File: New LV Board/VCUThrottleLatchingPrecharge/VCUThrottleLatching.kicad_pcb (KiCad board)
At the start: 2 copper layers, 46 x 50.5 mm, 32 parts, among them J1 B12B-PH-K-S:JST_B12B-PH-K-S, P1 PH1-20-UA, P2 PH1-20-UA, Q1 SS8550, U1 IRLML2060TRPBF, U2 IRLML2060TRPBF, U3 IRLML2060TRPBF, U5 IRLML2060TRPBF, U6 IRLML2060TRPBF, U8 PMV160UP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

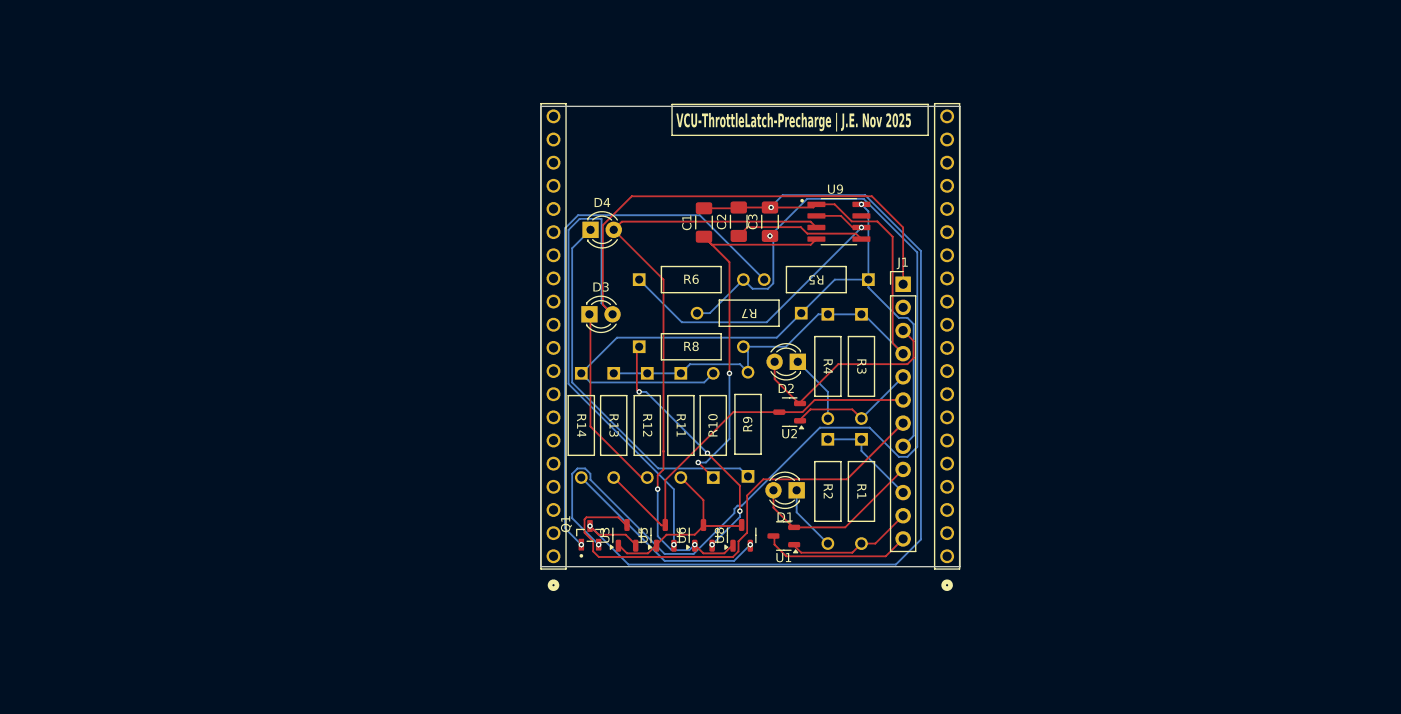
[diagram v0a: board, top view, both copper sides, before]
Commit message: VCU Latch and Precharge Schematic Update + Footprint Adjustments
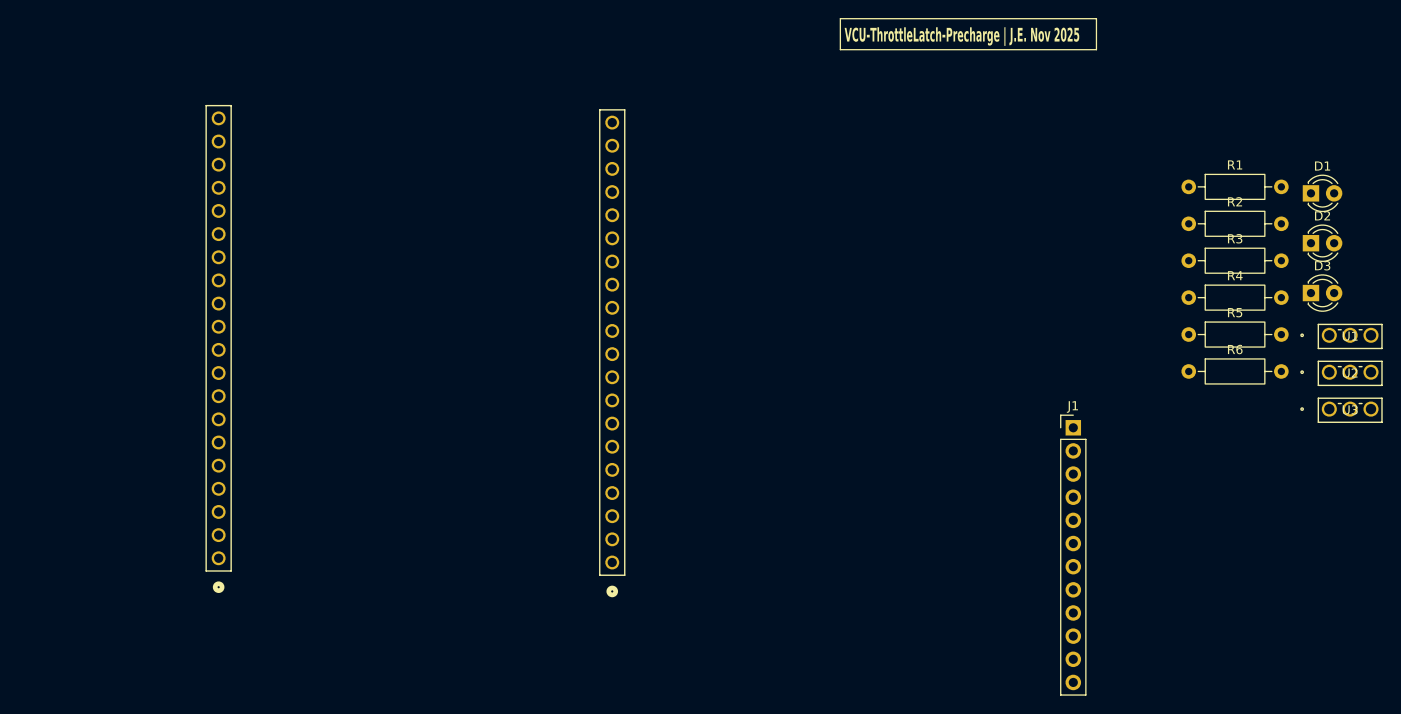
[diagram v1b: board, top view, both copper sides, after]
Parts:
- removed C1, C2: 0.1u, Capacitor_SMD:C_1206_3216Metric_Pad1.33x1.80mm_HandSolder
- removed C3: 47u, Capacitor_SMD:C_1206_3216Metric_Pad1.33x1.80mm_HandSolder
- removed D4: 3 second timer, LED_THT:LED_D3.0mm
- removed Q1: SS8550, Footprints:SOT95P237X112-3N
- removed R10: 22k, Footprints:STA_CF14_STP
- removed R11, R13: 10k, Footprints:STA_CF14_STP
- removed R12: 150R, Footprints:STA_CF14_STP
- removed R14: 2k, Footprints:STA_CF14_STP
- removed R7: 57.6k, Footprints:STA_CF14_STP
- removed R8: 500, Footprints:STA_CF14_STP
- removed R9: 1k, Footprints:STA_CF14_STP
- removed U5, U6: IRLML2060TRPBF, Package_TO_SOT_SMD:SOT-23-3
- removed U8: PMV160UP, Package_TO_SOT_SMD:SOT-23-3
- removed U9: NE555D, Footprints:SOIC127P599X175-8N
- R1, R2, R3, R4: footprint Footprints:STA_CF14_STP -> Resistor_THT:R_Axial_DIN0207_L6.3mm_D2.5mm_P10.16mm_Horizontal
- R5: value 1k -> 10k; footprint Footprints:STA_CF14_STP -> Resistor_THT:R_Axial_DIN0207_L6.3mm_D2.5mm_P10.16mm_Horizontal
- R6: value 1k -> 150R; footprint Footprints:STA_CF14_STP -> Resistor_THT:R_Axial_DIN0207_L6.3mm_D2.5mm_P10.16mm_Horizontal
- U1, U2, U3: footprint Package_TO_SOT_SMD:SOT-23-3 -> Motorsports:DPAK-3_6P35X6P73_ONS
- moved D3 79.2 mm to (221.7, 99.5)
- moved U3 78.3 mm to (223.7, 112.2), turned to 0 degrees
- moved D1 65.2 mm to (221.7, 88.6), turned to 0 degrees
- moved U1 63.8 mm to (223.7, 104.2), turned to 0 degrees
- moved R6 61.1 mm to (208.2, 108.1)
- moved U2 59.4 mm to (223.7, 108.2), turned to 0 degrees
- moved D2 57.8 mm to (221.7, 94.1), turned to 0 degrees
- moved R2 46.1 mm to (208.2, 91.9), turned to 0 degrees
- moved R1 45.3 mm to (208.2, 87.9), turned to 0 degrees
- moved R4 39.6 mm to (208.2, 100.0), turned to 0 degrees
- moved P2 36.7 mm to (145.0, 129.1)
- moved P1 36.7 mm to (101.8, 128.6)
- moved R3 36.4 mm to (208.2, 96.0), turned to 0 degrees
- moved R5 35.7 mm to (208.2, 104.1), turned to 0 degrees
- moved J1 24.4 mm to (195.6, 114.3)
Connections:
- J1 pad 10: Net-(Q1-C) -> unconnected-(J1-Pad10)
- J1 pad 11: Net-(U1-G) -> unconnected-(J1-Pad11)
- J1 pad 12: Net-(U1-D) -> unconnected-(J1-Pad12)
- J1 pad 2: unconnected-(J1-Pad2) -> Net-(U3-G)
- J1 pad 4: Net-(Q1-C) -> Net-(U2-G)
- J1 pad 5: Net-(U2-G) -> Net-(D1-A)
- J1 pad 6: Net-(U1-D) -> Net-(U1-G)
- J1 pad 7: Net-(U3-D) -> Net-(J1-Pad7)
- J1 pad 8: Net-(U9-VCC) -> Net-(U1-D)
- J1 pad 9: Net-(D1-A) -> unconnected-(J1-Pad9)
- R1 pad 1: Net-(Q1-C) -> Net-(J1-Pad7)
- R2 pad 1: Net-(Q1-C) -> Net-(J1-Pad7)
- R3 pad 1: Net-(Q1-C) -> Net-(J1-Pad7)
- R4 pad 1: Net-(Q1-C) -> Net-(J1-Pad7)
- R5 pad 1: Net-(U9-VCC) -> Net-(J1-Pad7)
- R5 pad 2: Net-(Q1-B) -> Net-(U3-G)
- R6 pad 1: Net-(U9-THR) -> Net-(J1-Pad7)
- R6 pad 2: Net-(Q1-E) -> Net-(D3-K)
- U3 pad 2: Net-(Q1-C) -> Net-(D3-A)
- U3 pad 3: Net-(U3-D) -> Net-(U1-D)
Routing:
- net Net-(Q1-C): track 182.8 -> 0.00 mm, vias 2 -> 0
- net Net-(Q1-E): track 116.7 -> 0.00 mm, vias 2 -> 0
- net Net-(D3-A): track 106.5 -> 0.00 mm, vias 1 -> 0
- net Net-(U9-VCC): track 81.0 -> 0.00 mm, vias 1 -> 0
- net Net-(D4-A): track 69.1 -> 0.00 mm, vias 2 -> 0
- net Net-(Q1-B): track 60.8 -> 0.00 mm, vias 1 -> 0
- net Net-(U1-D): track 59.0 -> 0.00 mm
- net Net-(U3-D): track 52.4 -> 0.00 mm
- net Net-(U9-R): track 43.1 -> 0.00 mm, vias 2 -> 0
- net Net-(D4-K): track 41.1 -> 0.00 mm
- net Net-(U9-THR): track 36.1 -> 0.00 mm, vias 1 -> 0
- net Net-(U6-S): track 28.2 -> 0.00 mm, vias 4 -> 0
- net Net-(D2-A): track 23.8 -> 0.00 mm
- net Net-(U8-S): track 23.1 -> 0.00 mm, vias 1 -> 0
- net Net-(U3-G): track 21.5 -> 0.00 mm
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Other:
- board outline removed

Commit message: throttle lathcing done I hope
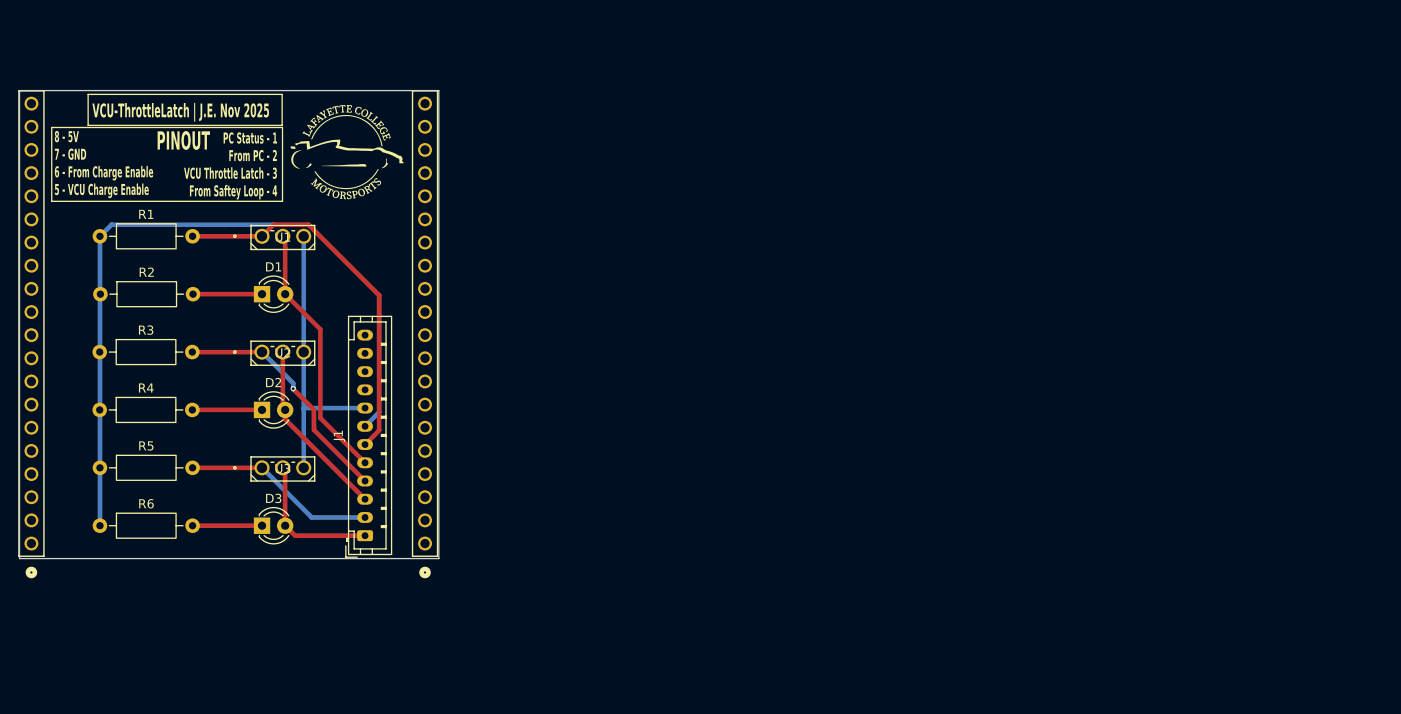
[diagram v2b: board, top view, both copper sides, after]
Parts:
- J1: footprint Connector_PinHeader_2.54mm:PinHeader_1x12_P2.54mm_Vertical -> Connector_JST:JST_PH_B12B-PH-K_1x12_P2.00mm_Vertical
- moved R6 120.6 mm to (88.8, 125.0)
- moved R5 120.3 mm to (88.8, 118.7)
- moved R4 120.1 mm to (88.8, 112.3)
- moved R3 119.9 mm to (88.8, 106.0)
- moved R2 119.6 mm to (88.8, 99.6)
- moved R1 119.6 mm to (88.8, 93.3)
- moved D3 117.9 mm to (106.6, 125.0)
- moved U1 117.6 mm to (106.6, 93.3)
- moved U3 117.3 mm to (106.6, 118.7)
- moved U2 117.1 mm to (106.6, 106.0)
- moved D2 116.5 mm to (106.6, 112.3)
- moved D1 115.6 mm to (106.6, 99.6)
- moved J1 78.6 mm to (117.9, 126.1), turned to 90 degrees
- moved P2 63.8 mm to (81.3, 127.0)
- moved P1 22.7 mm to (124.5, 127.0)
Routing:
- net Net-(J1-Pad7): track 0.00 -> 81.1 mm
- net Net-(U1-G): track 0.00 -> 41.1 mm
- net Net-(U1-D): track 0.00 -> 32.1 mm
- net Net-(D1-A): track 0.00 -> 28.6 mm
- net Net-(U2-G): track 0.00 -> 26.4 mm, vias 0 -> 1
- net Net-(U3-G): track 0.00 -> 21.2 mm
- net Net-(D2-A): track 0.00 -> 19.9 mm
- net Net-(D3-A): track 0.00 -> 15.7 mm
- net Net-(D2-K): track 0.00 -> 7.65 mm
- net Net-(D3-K): track 0.00 -> 7.62 mm
- net Net-(D1-K): track 0.00 -> 7.57 mm
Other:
- board outline added: 46 x 51.3 mm
- board text added: "8 - 5V 7 - GND 6 - From Charge Enable 5 - VCU Charge Enable"
- board text added: "PC Status - 1 From PC - 2 VCU Throttle Latch - 3 From Saftey Loop - 4"
- board text added: "PINOUT"
- board text added: "VCU-ThrottleLatch | J.E. Nov 2025"
- board text removed: "VCU-ThrottleLatch-Precharge | J.E. Nov 2025"

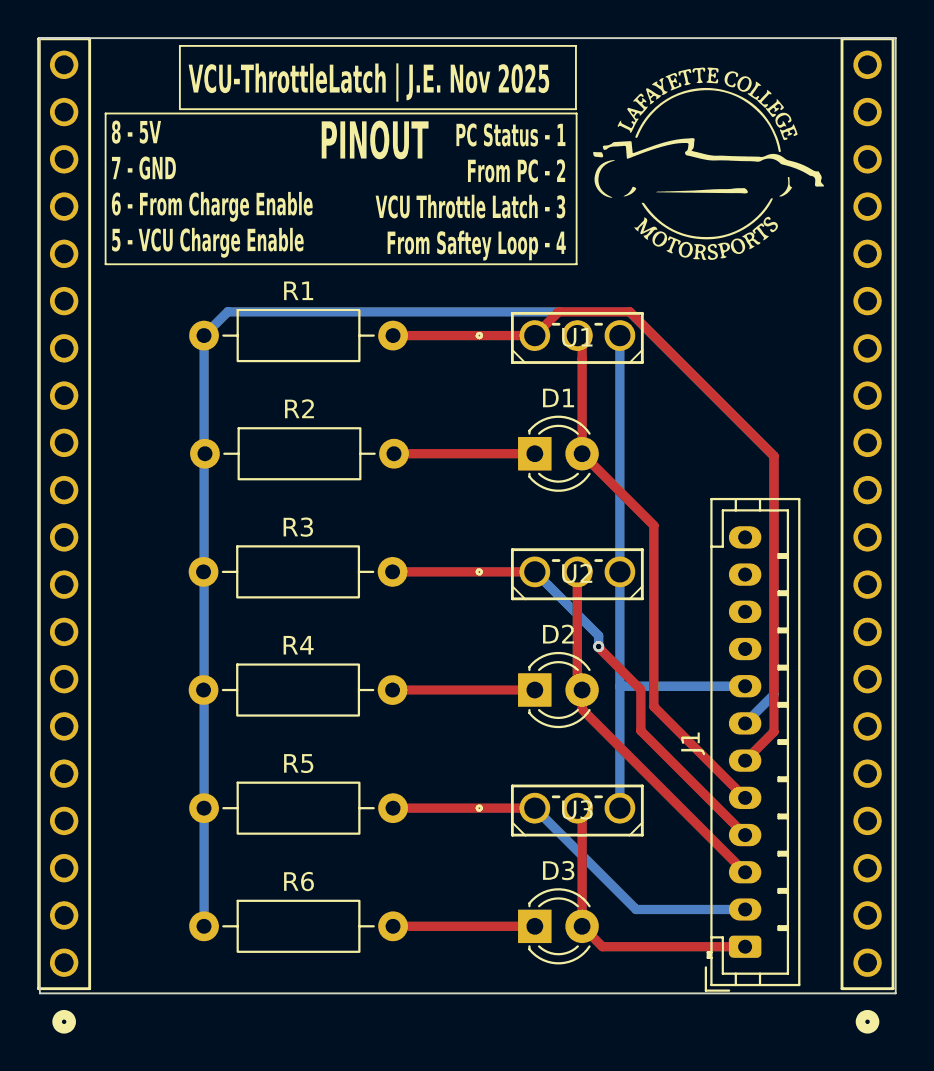
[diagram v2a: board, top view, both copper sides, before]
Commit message: made layout smaller to have space for hall effect and added better silkscreen
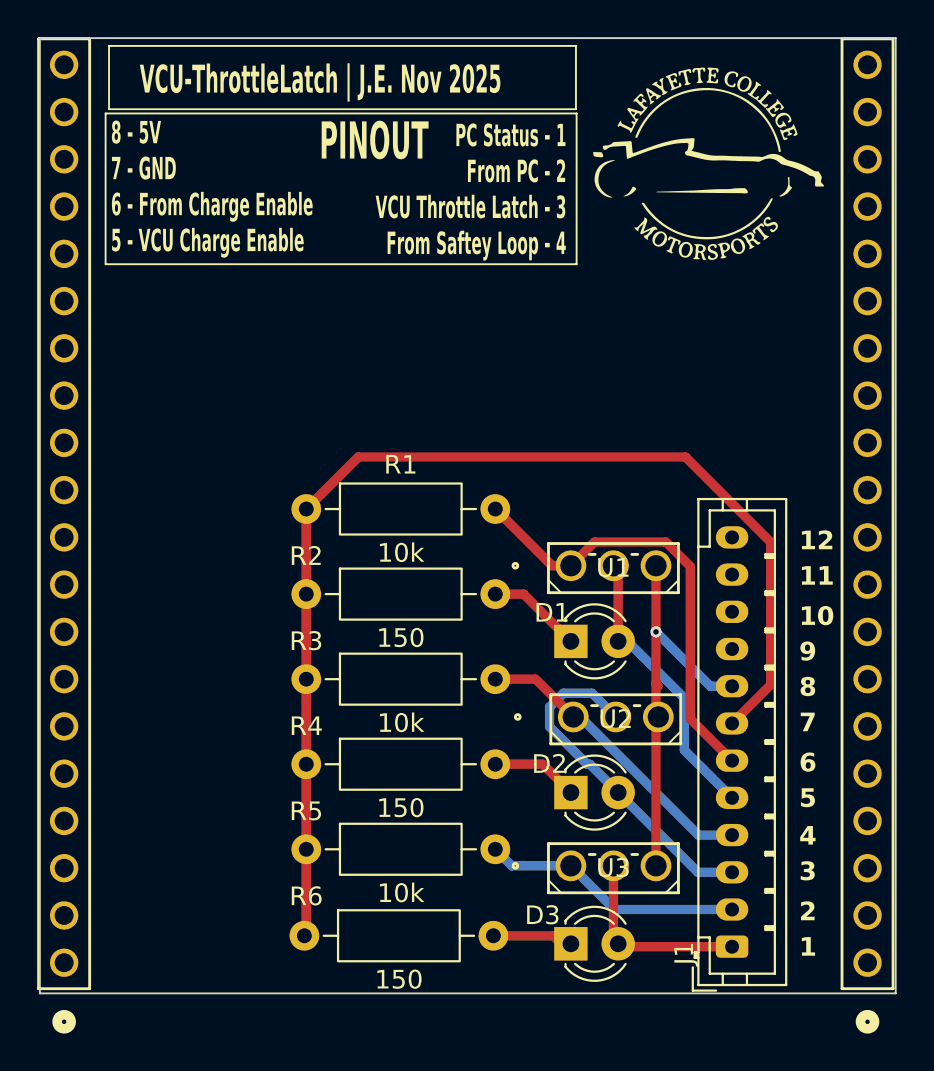
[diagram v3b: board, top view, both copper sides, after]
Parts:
- R2, R4, R6: value 150R -> 150
- moved U1 12.5 mm to (108.5, 105.7)
- moved R1 10.8 mm to (94.3, 102.6)
- moved D1 10.3 mm to (108.5, 109.7)
- moved R2 9.30 mm to (94.3, 107.2)
- moved U2 8.07 mm to (108.6, 113.8)
- moved R3 7.98 mm to (94.3, 111.8)
- moved R4 6.81 mm to (94.3, 116.3)
- moved R5 5.92 mm to (94.3, 120.9)
- moved D2 5.84 mm to (108.5, 117.9)
- moved R6 5.42 mm to (94.2, 125.6)
- moved U3 3.66 mm to (108.5, 121.8)
- moved D3 2.15 mm to (108.5, 126.0)
- moved J1 0.70 mm to (117.2, 126.1)
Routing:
- net Net-(J1-Pad7): track 81.1 -> 61.6 mm
- net Net-(U1-G): track 41.1 -> 24.2 mm
- net Net-(D1-A): track 28.6 -> 15.4 mm
- net Net-(U1-D): track 32.1 -> 21.6 mm, vias 0 -> 1
- net Net-(U2-G): track 26.4 -> 16.2 mm, vias 1 -> 0
- net Net-(U3-G): track 21.2 -> 14.1 mm
- net Net-(D3-A): track 15.7 -> 10.5 mm
- net Net-(D3-K): track 7.62 -> 4.34 mm
- net Net-(D2-K): track 7.65 -> 4.70 mm
- net Net-(D1-K): track 7.57 -> 5.12 mm
- net Net-(D2-A): track 19.9 -> 18.5 mm
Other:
- board text added: "1"
- board text added: "10"
- board text added: "11"
- board text added: "12"
- board text added: "2"
- board text added: "3"
- board text added: "4"
- board text added: "5"
- board text added: "6"
- board text added: "7"
- board text added: "8"
- board text added: "9"
